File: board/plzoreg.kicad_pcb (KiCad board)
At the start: 2 copper layers, 55 parts, among them J1 IN, J2 OUT, J3 Heatsink Earth, Q1 BTA24-600C, U1 HLK-PM03, U2 H11AA1, U3 MOC3023M, U4 PY32F030K1xTx, X1 SWD

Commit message: WIP
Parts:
- removed the D2 at (162.5, 82.2)
- removed D3: DSK14, Diode_SMD:D_SOD-123
- added C14: 100n, Capacitor_SMD:C_0805_2012Metric_Pad1.18x1.45mm_HandSolder, F.Cu at (136.7, 93.8)
- added H1: MountingHole, MountingHole:MountingHole_4.3mm_M4_Pad_Via, F.Cu at (81.2, 55.8)
- added H2: MountingHole, MountingHole:MountingHole_4.3mm_M4_Pad_Via, F.Cu at (81.2, 145.8)
- added H3: MountingHole, MountingHole:MountingHole_4.3mm_M4_Pad_Via, F.Cu at (171.2, 145.8)
- added H4: MountingHole, MountingHole:MountingHole_4.3mm_M4_Pad_Via, F.Cu at (171.2, 55.8)
- added R19: 47k 1%, Resistor_SMD:R_0805_2012Metric_Pad1.20x1.40mm_HandSolder, F.Cu at (136.7, 88.8)
- added R20: 1k5, Resistor_SMD:R_0805_2012Metric_Pad1.20x1.40mm_HandSolder, F.Cu at (136.7, 91.3)
- added TH1: 3950, Connector_PinHeader_2.54mm:PinHeader_1x02_P2.54mm_Vertical, F.Cu at (127.5, 90.8)
- added TP6: TSENSE, TestPoint:TestPoint_THTPad_D2.0mm_Drill1.0mm, F.Cu at (140.7, 93.8)
- J3: footprint Connector_Pin:Pin_D1.0mm_L10.0mm -> Connector_Wire:SolderWire-1.5sqmm_1x01_D1.7mm_OD3.9mm
- Q1: moved to B.Cu
- R7: footprint Resistor_SMD:R_0805_2012Metric_Pad1.20x1.40mm_HandSolder -> Resistor_THT:R_Axial_DIN0207_L6.3mm_D2.5mm_P10.16mm_Horizontal
- TP5: value ADC -> VSENSE
- moved R5 97.9 mm to (111.2, 122.2), turned to 90 degrees
- moved R2 95.5 mm to (101.2, 107.2), turned to 90 degrees
- moved R18 92.6 mm to (97.7, 54.3)
- moved J2 91.2 mm to (132.2, 128.6)
- moved R3 89.2 mm to (106.2, 107.2), turned to 90 degrees
- moved R17 88.3 mm to (97.7, 56.3)
- moved U1 86.2 mm to (87.2, 95.8), turned to 90 degrees
- moved R16 84.2 mm to (97.7, 58.3)
- moved R6 83.5 mm to (117.2, 109.5), turned to -90 degrees
- moved R10 82.1 mm to (85.7, 61.3)
- moved R15 80.1 mm to (97.7, 60.3)
- moved X1 80.0 mm to (79.7, 69.8), turned to -90 degrees
- moved R4 79.4 mm to (113.5, 89.8), turned to 180 degrees
- moved C9 78.8 mm to (81.7, 63.3), turned to 90 degrees
- moved C8 78.7 mm to (79.2, 63.3), turned to 90 degrees
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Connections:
- J1 pad 1: /MAIN_PEN -> /MAINS_L_IN
- J1 pad 3: /MAINS_L_IN -> /MAIN_PE
- J2 pad 1: /MAIN_PEN -> /MAIN_PE
- J3 pad 1: /MAIN_PEN -> /MAIN_PE
- R10 pad 2: /ADC -> /VSENSE
- TP5 pad 1: Net-(D1-K) -> /VSENSE
- U4 pad 14: /ADC -> /VSENSE
- U4 pad 15: /ZCD -> /TSENSE
- U4 pad 20: unconnected-(U4-PA10-OSC32IN-Pad20) -> /ZCD
- U4 pad 26: /DISP_CC1 -> unconnected-(U4-PB3-Pad26)
- U4 pad 27: /DISP_CC2 -> /DISP_CC3
- U4 pad 28: /DISP_CC3 -> /DISP_CC2
- U4 pad 5: unconnected-(U4-PF3-Pad5) -> /DISP_CC1
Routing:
- net VCC: track 0.00 -> 186.8 mm, vias 0 -> 3
- net /MAINS_N: track 0.00 -> 144.0 mm
- net /TRIAC: track 0.00 -> 117.6 mm, vias 0 -> 2
- net /BTN2: track 0.00 -> 115.0 mm, vias 0 -> 2
- net /MAINS_L_IN: track 0.00 -> 103.9 mm
- net /TSENSE: track 0.00 -> 102.0 mm
- net /BTN1: track 0.00 -> 98.1 mm, vias 0 -> 2
- net /DISP_CC3: track 0.00 -> 78.8 mm
- net /ZCD: track 0.00 -> 76.6 mm, vias 0 -> 2
- net /DISP_AP: track 0.00 -> 74.8 mm, vias 0 -> 2
- net /DISP_AC: track 0.00 -> 65.6 mm, vias 0 -> 3
- net /DISP_CC2: track 0.00 -> 64.9 mm
- net /DISP_AB: track 0.00 -> 61.6 mm, vias 0 -> 3
- net /DISP_AD: track 0.00 -> 60.5 mm, vias 0 -> 3
- net /DISP_AE: track 0.00 -> 57.9 mm, vias 0 -> 2
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- added copper zone on B.Cu, net GND
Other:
- board outline added: 100 x 100 mm

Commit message: WIP
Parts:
- J3: value Heatsink Earth -> Heatsink PE
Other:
- board text added: "DANGER"
- board text added: "HIGH VOLTAGE!"
- board text added: "INPUT"
- board text added: "L"
- board text added: "N"
- board text added: "OUTPUT"
- board text added: "PE"
- board text added: "PLZoREG"
- board text added: "drake.cz"
- board text added: "v1.0"

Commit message: WIP
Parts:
- removed the C4 at (99.2, 84.8)
- removed D1: DSK14, Diode_SMD:D_SOD-123
- removed D2: BAT54S, Package_TO_SOT_SMD:SOT-23
- removed the R4 at (113.5, 89.8)
- added R9: 10k, Resistor_SMD:R_0805_2012Metric_Pad1.20x1.40mm_HandSolder, F.Cu at (104.2, 89.8)
- added U3: LTV-817S, Package_DIP:SMDIP-4_W9.53mm, F.Cu at (104.2, 100.8)
- C4: renamed from C6; value 100n -> 1u
- R4: renamed from R2; value 510k/0.5W -> 330k/0.5W
- R5: renamed from R3; value 510k/0.5W -> 330k/0.5W
- moved R4 15.0 mm to (101.2, 122.2)
- moved R5 15.0 mm to (106.2, 122.2)
- moved C4 8.38 mm to (104.2, 92.8), turned to 0 degrees
- moved R2 1.00 mm to (112.2, 122.2)
- renumbered C14 to C10, C7 to C6, C8 to C7, C9 to C8, C10 to C9, J3 to J2, J2 to J3, R19 to R11, R20 to R12, R11 to R13, R12 to R14, R13 to R15, R14 to R16, R15 to R17, R16 to R18, R17 to R19, R5 to R2, R18 to R20, R6 to R3, R7 to R6, R8 to R7, R9 to R8, U3 to U4, U4 to U5
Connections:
- R4 pad 1: /MAINS_L_IN -> /MAINS_N
- R5 pad 1: /MAINS_N -> /MAINS_L_IN
- R5 pad 2: GND -> Net-(R5-Pad2)
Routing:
- net /MAINS_L_IN: track 103.9 -> 88.2 mm
- net /MAINS_N: track 144.0 -> 156.0 mm
- net Net-(C4-Pad1): track 52.2 -> 60.2 mm
- net VCC: track 186.8 -> 193.3 mm
- net Net-(R4-Pad2): track 10.3 -> 4.60 mm
- net Net-(R5-Pad2): track 0.00 -> 4.19 mm
- net GND: track 30.3 -> 29.3 mm, vias 16 -> 15

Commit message: WIP
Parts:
- removed C13: 100n, Capacitor_SMD:C_0805_2012Metric_Pad1.18x1.45mm_HandSolder
- U5: value PY32F030K1xTx -> PY32F030K2xTx
- moved C9 4.37 mm to (97.7, 70.5), turned to 0 degrees
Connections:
- R13 pad 1: Net-(U5-PA0) -> Net-(U5-PB8)
- R14 pad 1: Net-(U5-PA1) -> Net-(U5-PA0)
- R15 pad 1: Net-(U5-PA2) -> Net-(U5-PA1)
- R16 pad 1: Net-(U5-PA3) -> Net-(U5-PA2)
- R17 pad 1: Net-(U5-PA4) -> Net-(U5-PA3)
- R18 pad 1: Net-(U5-PA5) -> Net-(U5-PA4)
- R19 pad 1: Net-(U5-PA6) -> Net-(U5-PA5)
- R20 pad 1: Net-(U5-PA7) -> Net-(U5-PA6)
- U5 pad 13: Net-(U5-PA7) -> unconnected-(U5-PA7-Pad13)
- U5 pad 17: VCC -> unconnected-(U5-PB2-Pad17)
- U5 pad 25: unconnected-(U5-PA15-Pad25) -> /DISP_CC1
- U5 pad 26: unconnected-(U5-PB3-Pad26) -> /DISP_CC2
- U5 pad 28: /DISP_CC2 -> unconnected-(U5-PB5-Pad28)
- U5 pad 32: GND -> Net-(U5-PB8)
- U5 pad 5: /DISP_CC1 -> unconnected-(U5-PF3-Pad5)
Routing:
- net Net-(U5-PA7): track 16.1 -> 0.00 mm
- net Net-(U5-PB8): track 0.00 -> 10.8 mm, vias 0 -> 2
- net /DISP_CC1: track 47.5 -> 56.7 mm, vias 0 -> 1
- net VCC: track 193.3 -> 188.4 mm
- net GND: track 29.3 -> 25.6 mm, vias 15 -> 13
- net /DISP_CC2: track 64.9 -> 68.5 mm, vias 0 -> 1
- net Net-(U5-PF2-NRST): track 7.36 -> 4.85 mm
- net /DISP_AG: track 51.8 -> 53.9 mm
- net Net-(U5-PA3): track 7.32 -> 8.88 mm
- net Net-(U5-PA2): track 5.03 -> 5.86 mm
- net Net-(U5-PA1): track 4.53 -> 5.36 mm
- net /DISP_AF: track 53.7 -> 53.2 mm
- net /ZCD: track 76.6 -> 77.2 mm
- net Net-(U5-PA4): track 9.95 -> 10.5 mm
- net Net-(C4-Pad1): vias 2 -> 0

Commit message: WIP
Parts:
- removed U2: H11AA1, Package_DIP:DIP-6_W8.89mm_SMDSocket_LongPads
- added U6: LTV-354T, Package_SO:SO-4_4.4x3.6mm_P2.54mm, F.Cu at (114.2, 100.8)
- C4: value 1u -> 10u
- R9: value 10k -> 1k5
- moved TP2 13.5 mm to (119.2, 90.8)
- moved C2 4.58 mm to (114.2, 94.8)
- moved R8 4.27 mm to (114.2, 91.8)
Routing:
- net /ZCD: track 77.2 -> 66.7 mm, vias 2 -> 4
- net Net-(R2-Pad2): track 4.40 -> 6.45 mm
- net GND: track 25.6 -> 26.8 mm, vias 13 -> 12
- net Net-(R3-Pad1): track 5.03 -> 6.22 mm
- net VCC: track 188.4 -> 188.2 mm, vias 3 -> 1

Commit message: WIP
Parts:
- added H5: MountingHole, MountingHole:MountingHole_3.7mm, F.Cu at (86.2, 133.8)
- added H6: MountingHole, MountingHole:MountingHole_3.7mm, F.Cu at (166.2, 133.8)
- moved C6 24.2 mm to (100.2, 86.3), turned to 0 degrees
- moved C7 21.9 mm to (97.7, 75.0), turned to 0 degrees
- moved C5 20.9 mm to (100.2, 83.8), turned to 0 degrees
- moved C8 18.6 mm to (97.7, 72.8), turned to 0 degrees
- moved C3 17.7 mm to (100.2, 81.3), turned to 0 degrees
- turned C4 to 180 degrees
- turned R9 to 0 degrees
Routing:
- net VCC: track 188.2 -> 168.6 mm, vias 1 -> 2
- net Net-(C4-Pad1): track 60.2 -> 62.2 mm

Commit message: WIP
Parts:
- added J4: AUX, Connector_IDC:IDC-Header_2x07_P2.54mm_Vertical, F.Cu at (121.6, 58.6)
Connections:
- U5 pad 13: unconnected-(U5-PA7-Pad13) -> /AUX_PA7
- U5 pad 17: unconnected-(U5-PB2-Pad17) -> /AUX_PB2
- U5 pad 19: unconnected-(U5-PA9-OSC32OUT-Pad19) -> /AUX_PA9
- U5 pad 2: unconnected-(U5-PF0-OSCIN-Pad2) -> /AUX_PF0
- U5 pad 28: unconnected-(U5-PB5-Pad28) -> /AUX_PB5
- U5 pad 29: unconnected-(U5-PB6-Pad29) -> /AUX_PB6
- U5 pad 3: unconnected-(U5-PF1-OSCOUT-Pad3) -> /AUX_PF1
- U5 pad 30: unconnected-(U5-PB7-Pad30) -> /AUX_PB7
- U5 pad 31: unconnected-(U5-PF4-BT0-Pad31) -> /AUX_PF4
- U5 pad 5: unconnected-(U5-PF3-Pad5) -> /AUX_PF3
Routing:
- net VCC: track 168.6 -> 233.2 mm
- net /AUX_PB5: track 0.00 -> 63.2 mm, vias 0 -> 1
- net /AUX_PB6: track 0.00 -> 59.5 mm, vias 0 -> 1
- net /AUX_PA7: track 0.00 -> 58.8 mm, vias 0 -> 1
- net /AUX_PB7: track 0.00 -> 56.3 mm, vias 0 -> 1
- net /AUX_PA9: track 0.00 -> 53.6 mm, vias 0 -> 1
- net /AUX_PF4: track 0.00 -> 52.9 mm, vias 0 -> 1
- net /AUX_PF3: track 0.00 -> 51.9 mm, vias 0 -> 1
- net /AUX_PF1: track 0.00 -> 51.3 mm, vias 0 -> 1
- net /AUX_PB2: track 0.00 -> 49.7 mm, vias 0 -> 1
- net /AUX_PF0: track 0.00 -> 48.4 mm, vias 0 -> 1
- net Net-(C4-Pad1): track 62.2 -> 66.9 mm
- net /BTN2: track 115.0 -> 112.9 mm
- net /BTN1: track 98.1 -> 96.3 mm
- net Net-(U5-PB8): track 10.8 -> 9.40 mm
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
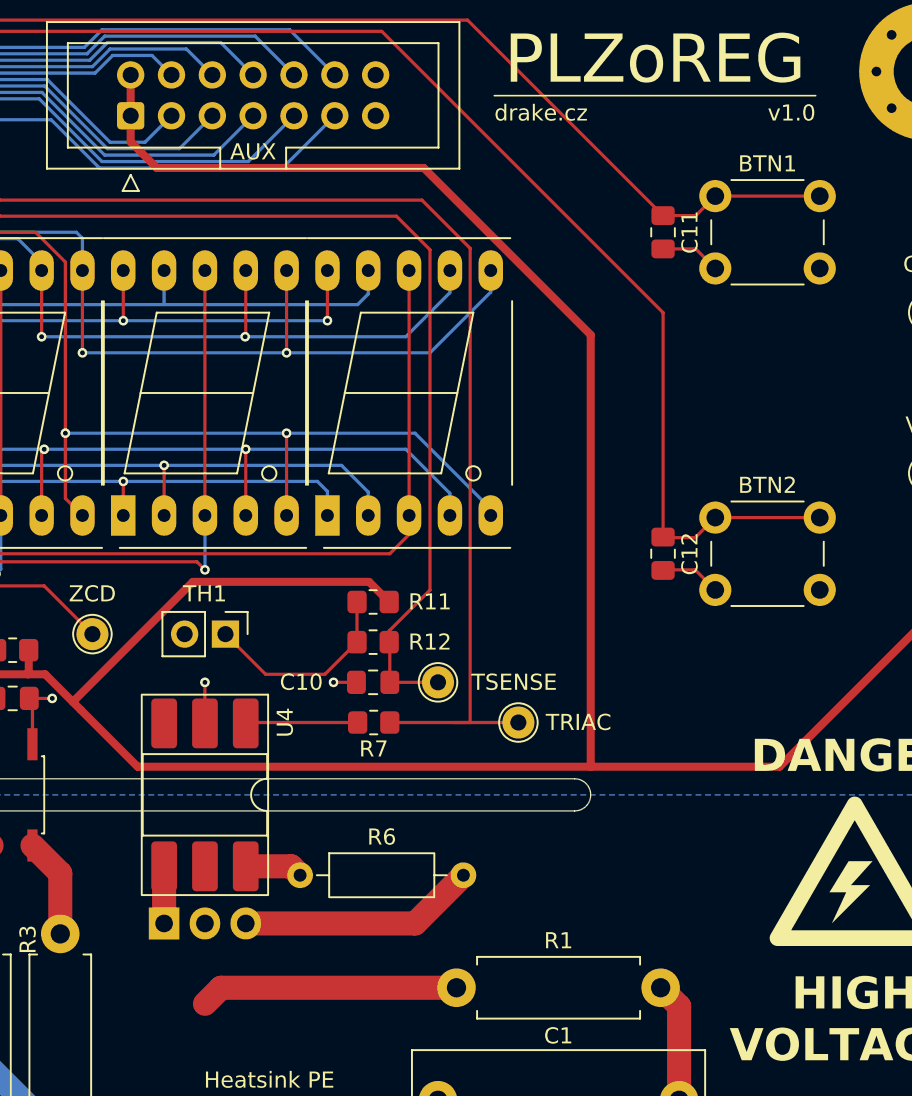
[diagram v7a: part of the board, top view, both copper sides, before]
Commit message: v1.1: fixed triac gate issue
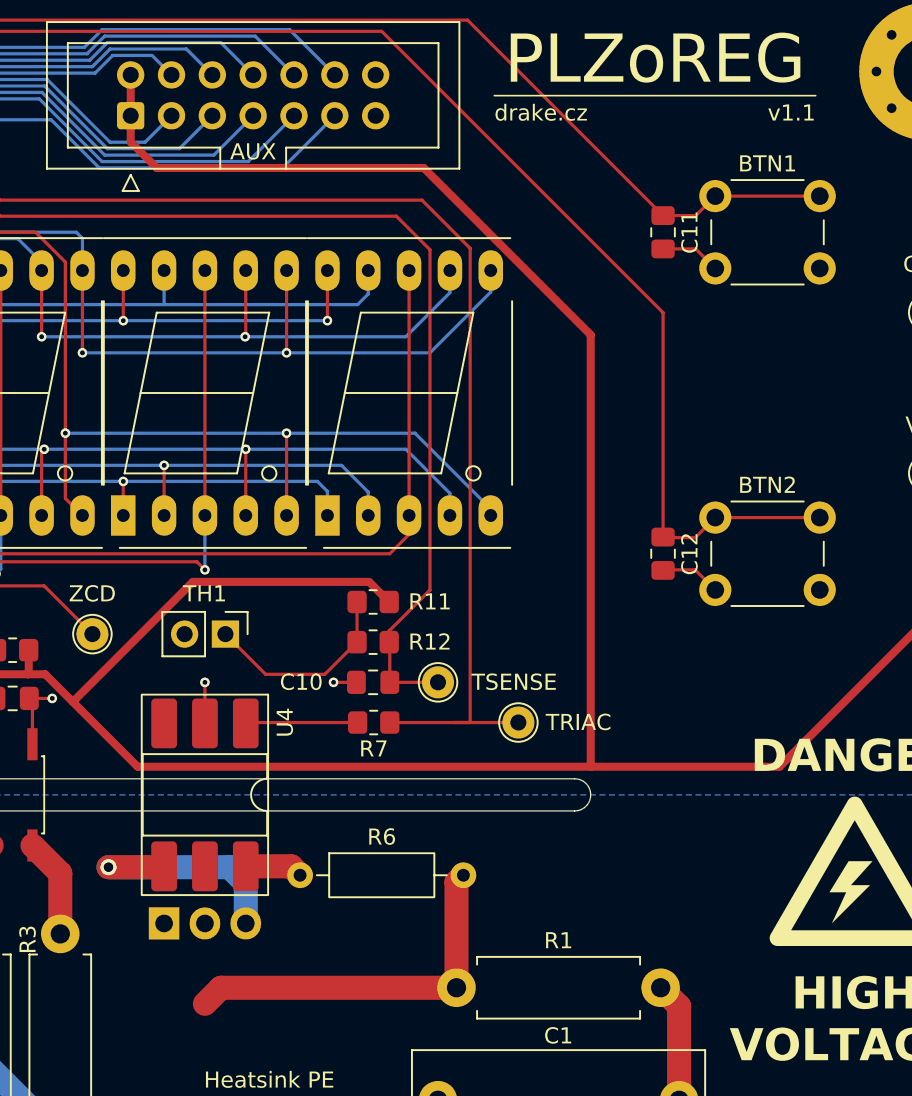
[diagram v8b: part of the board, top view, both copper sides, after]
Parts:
- R9: value 1k5 -> 10k
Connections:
- R6 pad 2: Net-(Q1-G) -> /MAINS_L_IN
- U4 pad 4: /MAINS_L_OUT -> Net-(Q1-G)
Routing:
- net /MAINS_L_IN: track 88.2 -> 95.3 mm
- net /MAINS_L_OUT: track 45.1 -> 41.6 mm
- net Net-(Q1-G): track 14.8 -> 14.9 mm, vias 0 -> 1
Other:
- board text added: "v1.1"
- board text removed: "v1.0"
